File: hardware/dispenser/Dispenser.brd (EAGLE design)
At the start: 73.7 x 75.6 mm, 70 parts, among them J1 AVR_Prog, J2 RJ45-8PTH, Q1 NFET-SO8, Q2 NFET, Q3 NFET, Q4 NFET, Q5 MOSFET-NCHANNELSMD, U1 ATMEGA168, U10 HALL-EFFECT, U2 OPAMP-DUAL, U3 OPTO-TLP185, U4 MPX5010DP, U5 VREG-5V-LDO-AP1117SOT89-3L, U6 WS2801, U7 HALL-EFFECT, U8 HALL-EFFECT, U9 HALL-EFFECT

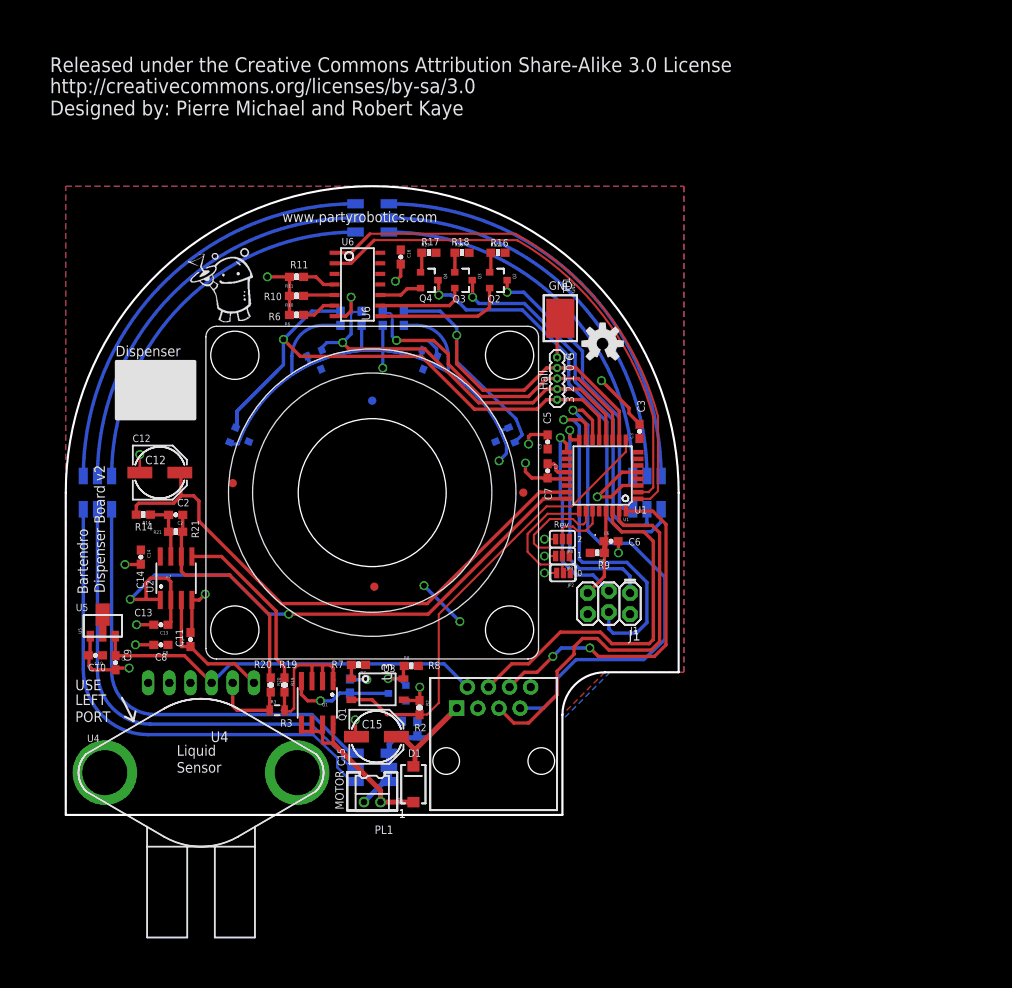
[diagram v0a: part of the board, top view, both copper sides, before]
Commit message: Remove annoying bottle size drop downs and fix changing dispense button
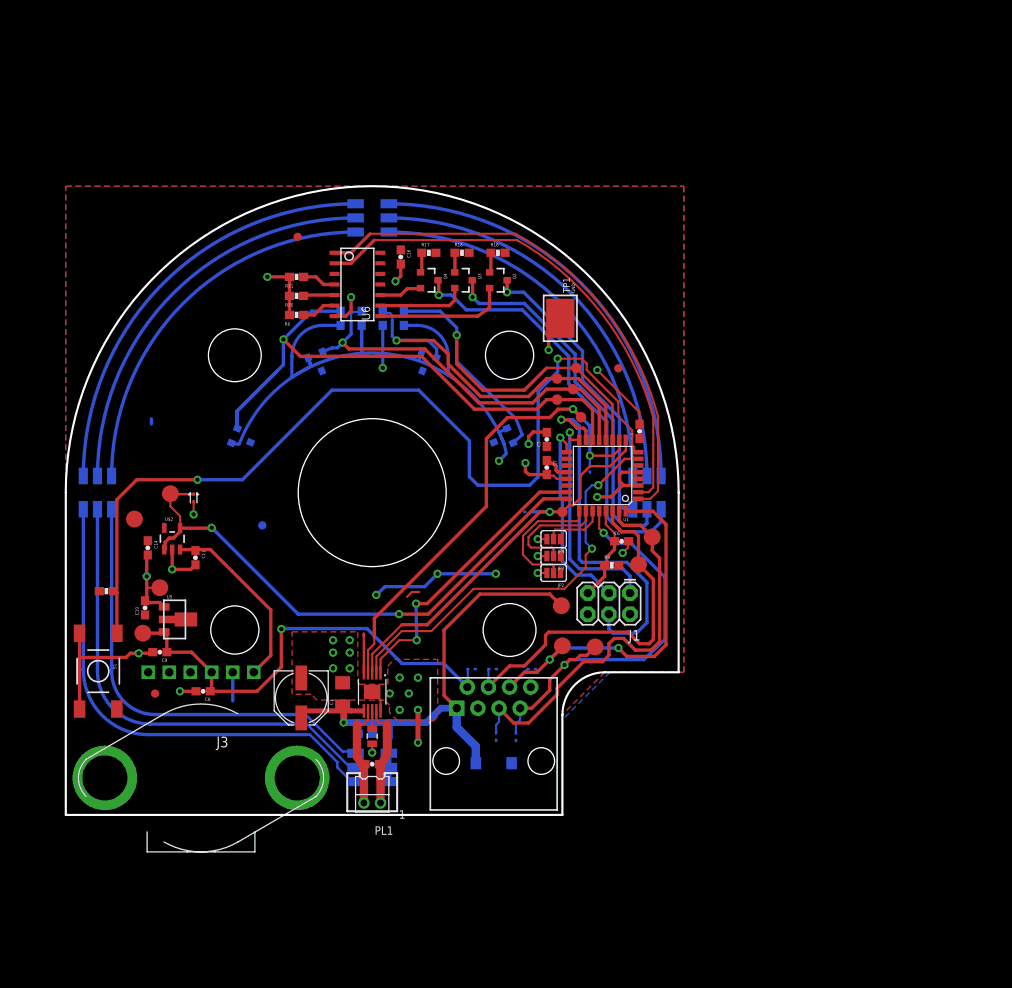
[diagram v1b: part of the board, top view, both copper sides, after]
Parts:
- removed C12: 100u 6.3V, SparkFun-Capacitors:PANASONIC_D
- removed C13: 100n, SparkFun:0603-CAP
- removed JP1: (no value), SparkFun:1X05-1.27MM
- removed Q1: NFET-SO8, pierre:SO08
- removed Q5: MOSFET-NCHANNELSMD, SparkFun-DiscreteSemi:SOT23-3
- removed R14, R19, R20: 1k, SparkFun-Resistors:0603-RES
- removed R2, R21: 10k, SparkFun-Resistors:0603-RES
- removed R7: 200, SparkFun-Resistors:0603-RES
- removed R8: 330, SparkFun-Resistors:0603-RES
- removed U2: OPAMP-DUAL, SparkFun-AnalogIC:SO08
- removed U4: MPX5010DP, pierre:MPX5010DP
- added D2, D3, D4, D6, D7, D8, D9: TVSSOD-923, pierre:SOD-923
- added D5: TVSSMA, pierre:SMA-DIODE
- added J3: MPX5010DPHDR, pierre:MPX5010_HDR
- added S1: (no value), pierre:TACTILE_SWITCH_SMD
- added TP10, TP11, TP12, TP7, TP8, TP9: TEST-POINT3X5, SparkFun-Passives:PAD.03X.05
- added TP13, TP14, TP15, TP16, TP2, TP3, TP4, TP5, TP6: TEST-POINT0.08, pierre:PAD_0.08
- added U$2: FAN4171, SparkFun-AnalogIC:SOT23-5
- C1: value 10u -> 10uF; device SparkFun-Passives:0603-CAP -> SparkFun-Capacitors:1206
- C15: value 47u 35V -> 47u 50V
- D1: value (none) -> TVSSOD-923; device pierre:SMA-DIODE -> pierre:SOD-923
- J1: value AVR_Prog -> AVR_SPI_PRG_6PTH; device SparkFun-Connectors:2X3_LOCK -> SparkFun-Connectors:2X3
- JP2: value JUMPER-32-3 -> JUMPER-31-2; device SparkFun-Passives:SJ_3_PASTE2&3 -> SparkFun-Passives:SJ_3_PASTE1&2
- R10: value 33 -> 39
- R11: value 33 -> 30
- R3: value 0.2 -> 0.24
- R6: value 33 -> 68
- U3: value OPTO-TLP185 -> A4952; device pierre:SO6 -> pierre:MSOP-10-GNDPAD
- moved C2 38.2 mm to (36.8, 6.10), turned to 0 degrees
- moved R1 31.4 mm to (4.89, 26.9), flipped to the top, turned to 180 degrees
- moved JP5 30.6 mm to (27.9, 69.5)
- moved JP8 29.3 mm to (10.7, 14.6)
- moved JP6 20.0 mm to (23.6, 34.8)
- moved D1 19.8 mm to (56.0, 17.5), flipped to the bottom, turned to 0 degrees
- moved JP7 18.8 mm to (66.4, 53.7)
- moved R3 11.8 mm to (36.8, 9.45), turned to 90 degrees
- moved C15 10.2 mm to (28.3, 14.1), turned to 270 degrees
- moved C11 9.85 mm to (15.6, 30.9), turned to 270 degrees
- moved U5 8.67 mm to (13.1, 23.5), turned to 270 degrees
- moved C10 8.26 mm to (9.53, 24.9), turned to 90 degrees
- moved C1 8.19 mm to (33.3, 14.5), flipped to the top
- moved C8 7.55 mm to (16.5, 14.9)
- moved C4 6.28 mm to (36.0, 9.75), turned to 180 degrees
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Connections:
- net R0 renamed REV0
- net R1 renamed REV1
- net R2 renamed REV2
- removed net 1/4W: Q1.1, Q1.2, Q1.3, R19.2, R3.2
- removed net CUR_SEN: C12.+, R14.2, U1.23
- removed net MOT_B: D1.A, PL1.1, Q1.5, Q1.6, Q1.7, Q1.8
- removed net MOT_CTL: R2.2, U1.9, U3.3
- removed net MOT_CUR: C2.2, R14.1, R21.1, U2.7
- removed net N$11: R19.1, U2.5
- removed net N$16: R7.2, U3.1
- removed net N$31: Q5.1, R8.1, U3.6
- new net 1/3W: R3.2, U3.8
- new net BUTTON: R1.1, S1.1, U1.8
- new net FAULT: U1.23, U3.1
- new net MOT_CTLA: D7.C, TP8.P$1, U1.10, U3.4
- new net MOT_CTLB: D8.C, TP7.P$1, U1.9, U3.3
- new net RTRY: U1.7, U3.2
- net 3.3V: now also TP16.P$1, U$2.5, U3.5; no longer C8.1, R7.1, R8.2, U2.8
- net 5V: now also C8.1, D4.C, J3.3, TP3.P$1; no longer U4.3
- net GND: now also D1.A, D2.A, D3.A, D4.A, D5.A, D6.A, D7.A, D8.A, D9.A, J3.2, S1.3, S1.4, TP2.P$1, U$2.2, U3.10, U3.GND; no longer C12.-, C13.2, JP1.1, Q5.2, R2.1, R20.2, U2.4, U3.4, U4.2
- net HALL0: now also TP10.P$1, U1.11; no longer JP1.2, U1.10
- net HALL1: now also TP11.P$1, U1.12; no longer JP1.3, U1.11
- net HALL2: now also TP9.P$1, U1.13; no longer JP1.4, U1.12
- net HALL3: now also TP12.P$1, U1.14; no longer JP1.5, U1.13
- net LIQ_LVL: now also D9.C, TP14.P$1, U$2.1, U$2.4; no longer C13.1, U2.1, U2.2
- net N$10: now also C2.2, PL1.1, U3.9; no longer C2.1, R20.1, R21.2, U2.6
- net N$26: now also J3.1, U$2.3; no longer U2.3, U4.1
- net N$9: now also C2.1, PL1.2, U3.7; no longer Q1.4, Q5.3, R1.1
- net RESET: now also D1.C, TP13.P$1
- net RX: now also D6.C, TP4.P$1
- net SYNC: now also D3.C, TP15.P$1, U1.28; no longer U1.14
- net TX: now also D2.C, TP5.P$1
- net VIN: now also D5.C, TP6.P$1, U3.6; no longer D1.C, PL1.2
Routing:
- net BUTTON: track 0.00 -> 112.7 mm, vias 0 -> 2
- net CUR_SEN: track 69.4 -> 0.00 mm
- net MOT_CTLA: track 0.00 -> 60.0 mm, vias 0 -> 2
- net MOT_CTL: track 54.5 -> 0.00 mm
- net RTRY: track 0.00 -> 49.2 mm, vias 0 -> 2
- net MOT_CTLB: track 0.00 -> 48.1 mm, vias 0 -> 1
- net VIN: track 38.5 -> 75.1 mm, vias 0 -> 1
- net FAULT: track 0.00 -> 35.0 mm, vias 0 -> 2
- net MOT_B: track 23.6 -> 0.00 mm
- net 3.3V: track 97.1 -> 118.7 mm
- net N$11: track 21.3 -> 0.00 mm
- net 1/4W: track 19.8 -> 0.00 mm
- net N$10: track 27.3 -> 14.1 mm
- net SYNC: track 61.4 -> 49.2 mm, vias 1 -> 2
- net GND: track 92.1 -> 100.9 mm, vias 19 -> 31
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- added copper zone on layer 1, net GND
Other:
- board text added: "24V"
- board text added: "3.3V"
- board text added: "5V"
- board text added: "D2"
- board text added: "D3"
- board text added: "D4"
- board text added: "D5"
- board text added: "D6"
- board text added: "D7"
- board text added: "D8"
- board text added: "Dispenser Board v3"
- board text added: "Dispenser#"
- board text added: "ID"
- board text added: "IN1"
- board text added: "IN2"
- board text added: "J3"
- board text added: "Level"
- board text added: "Liq"
- board text added: "Lvl"
- board text added: "RST"
- board text added: "RX"
- board text added: "SYNC"
- board text added: "TX"
- board text added: "button"
- board text removed: "C1"
- board text removed: "C12"
- board text removed: "C13"
- board text removed: "C15"
- board text removed: "C2"
- board text removed: "C4"
- board text removed: "Dispenser"
- board text removed: "Dispenser Board v2"
- board text removed: "G"
- board text removed: "Q1"
- board text removed: "Q5"
- board text removed: "R1"
- board text removed: "R14"
- board text removed: "R19"
- board text removed: "R2"
- board text removed: "R20"
- board text removed: "R21"
- board text removed: "R3"
- board text removed: "R7"
- board text removed: "R8"
- board text removed: "U3"
- board text removed: "U4"
